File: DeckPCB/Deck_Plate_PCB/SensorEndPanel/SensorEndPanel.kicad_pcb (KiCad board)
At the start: 2 copper layers, 127.3 x 19.1 mm, 11 parts, among them J1 Board_to_Board, U1 LM20, U2 PiCam

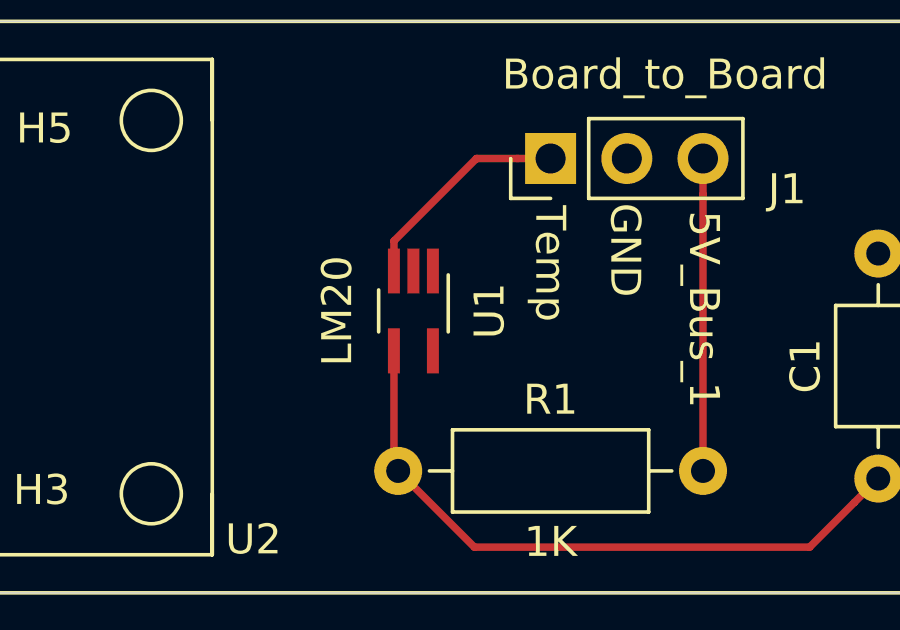
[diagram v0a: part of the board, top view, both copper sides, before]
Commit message: Updated Main_Deck_Plate and Daughter_Board to fit Electronics Enclosure internal dimensions. Created all PCB Gerber files. Created all PCB PNG images. Created all PCB STEP files for mechanical integration. Implemented all design review comments and corrections.
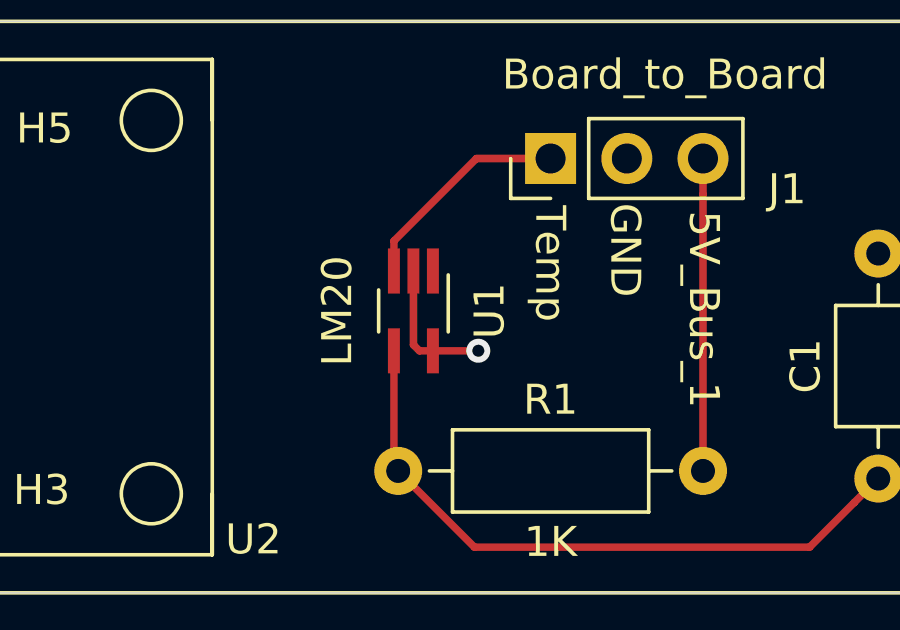
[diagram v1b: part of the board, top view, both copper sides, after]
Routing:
- net GND: track 0.00 -> 4.71 mm, vias 0 -> 1
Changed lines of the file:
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@@
     (thickness 1.6)
     (drawings 14)
-    (tracks 12)
+    (tracks 18)
     (zones 0)
     (modules 11)
@@
     (solder_mask_min_width 0.25)
     (aux_axis_origin 0 0)
-    (visible_elements FFFFFF7F)
+    (visible_elements 7FFFFFFF)
     (pcbplotparams
       (layerselection 0x010fc_ffffffff)
@@
   (gr_line (start 175.514 25.4) (end 175.514 44.45) (layer F.SilkS) (width 0.12))
   (gr_line (start 48.26 25.4) (end 175.514 25.4) (layer F.SilkS) (width 0.12))
+  (via (at 133.48 36.38) (size 0.8) (drill 0.4) (layers F.Cu B.Cu) (net 1))
+  (segment (start 131.968 36.382) (end 133.478 36.382) (width 0.25) (layer F.Cu) (net 1))
+  (segment (start 133.478 36.382) (end 133.48 36.38) (width 0.25) (layer F.Cu) (net 1))
+  (segment (start 131.518 36.382) (end 131.968 36.382) (width 0.25) (layer F.Cu) (net 1))
+  (segment (start 131.318 33.722) (end 131.318 36.182) (width 0.25) (layer F.Cu) (net 1))
+  (segment (start 131.318 36.182) (end 131.518 36.382) (width 0.25) (layer F.Cu) (net 1))
   (segment (start 130.668 40.244) (end 130.81 40.386) (width 0.25) (layer F.Cu) (net 2))
   (segment (start 130.668 36.382) (end 130.668 40.244) (width 0.25) (layer F.Cu) (net 2))
